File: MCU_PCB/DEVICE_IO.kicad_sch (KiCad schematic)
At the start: 3 parts

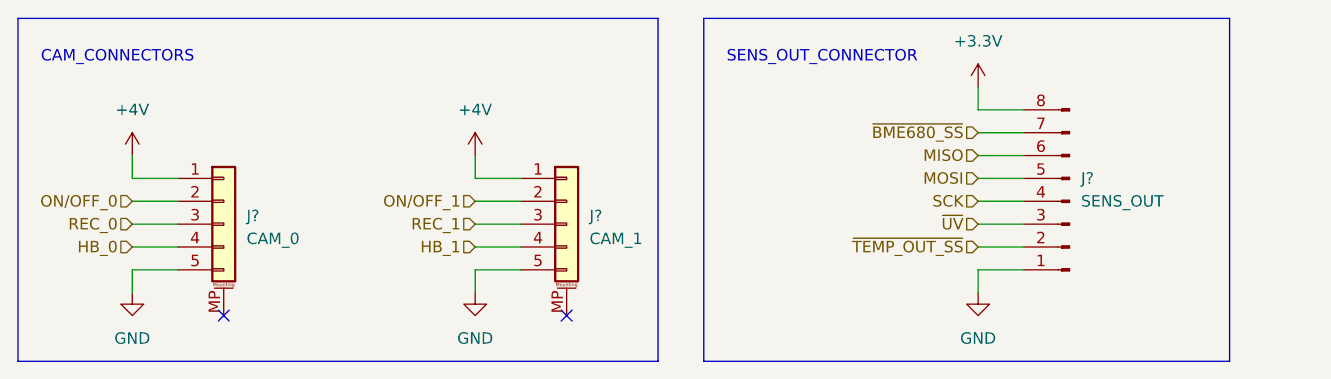
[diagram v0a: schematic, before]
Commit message: 0.1v MCU KiCad
Aesthetics needs to be improved.
Trace width needs to be changed.
More sufficient grounding.
Component placement could be changed.
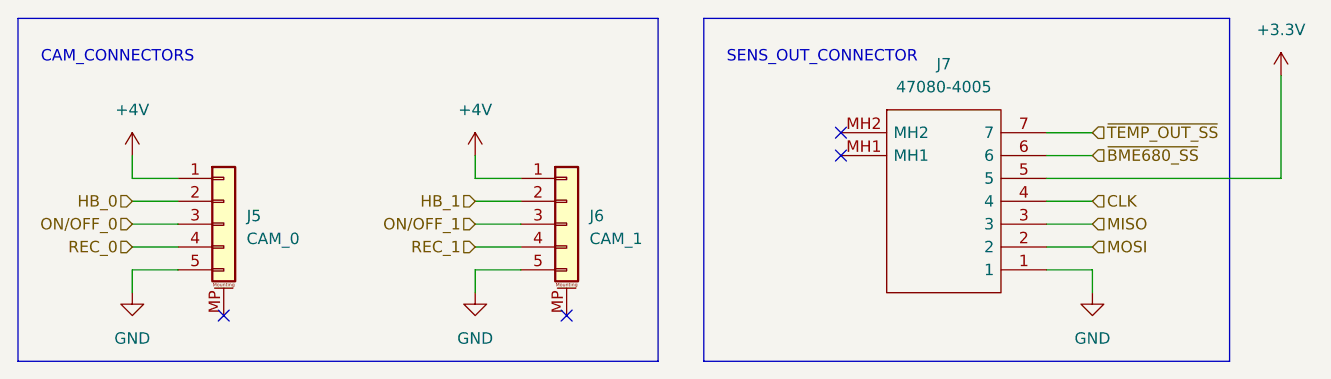
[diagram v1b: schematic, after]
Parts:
- removed J?: SENS_OUT, symbol Connector:Conn_01x08_Male
- added J7: 47080-4005, footprints:470804005, symbol schematics:47080-4005
- gave numbers to parts that had none: 2
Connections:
- net +3V3: now also J7.5
- net GND: now also J7.1
- net HB_0: now also J5.2 (Pin_2); no longer J5.4 (Pin_4)
- net HB_1: now also J6.2 (Pin_2); no longer J6.4 (Pin_4)
- net MISO: now also J7.3
- net MOSI: now also J7.2
- net ON/OFF_0: now also J5.3 (Pin_3); no longer J5.2 (Pin_2)
- net ON/OFF_1: now also J6.3 (Pin_3); no longer J6.2 (Pin_2)
- net REC_0: now also J5.4 (Pin_4); no longer J5.3 (Pin_3)
- net REC_1: now also J6.4 (Pin_4); no longer J6.3 (Pin_3)
- net ~{BME680_SS}: now also J7.6
- net ~{TEMP_OUT_SS}: now also J7.7
- new net CLK: J7.4
- no-connect marks 2 -> 4
